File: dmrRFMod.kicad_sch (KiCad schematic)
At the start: 14 parts, among them U2 AX.25 Module (DMR818SU)

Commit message: Added 3D models to all components except DMR module, need to make a 3D model for that one.
Signed-off-by: Logan Tolbert <xem6df@virginia.edu>
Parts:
- R3: footprint R_10OHM:RESC1005X40 -> R_220O:RESC6332X70N
- R4: footprint Resistor_SMD:R_0805_2012Metric -> R_10kO:RESC1005X40N
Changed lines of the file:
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@@
 			)
 		)
-		(property "Footprint" "R_10OHM:RESC1005X40"
+		(property "Footprint" "R_220O:RESC6332X70N"
 			(at 110.236 95.504 90)
 			(effects
@@
 			)
 		)
-		(property "Footprint" "Resistor_SMD:R_0805_2012Metric"
+		(property "Footprint" "R_10kO:RESC1005X40N"
 			(at 129.794 70.866 90)
 			(effects

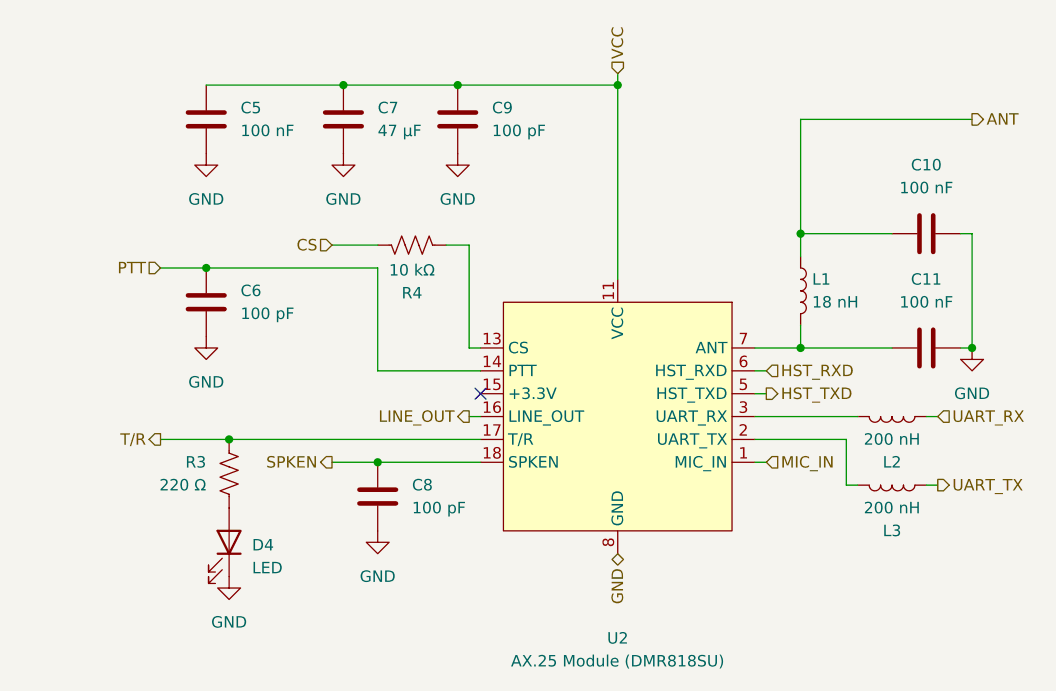
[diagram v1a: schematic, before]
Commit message: removed extraneous connections to the XBee and DMR modules on schematic and PCB.
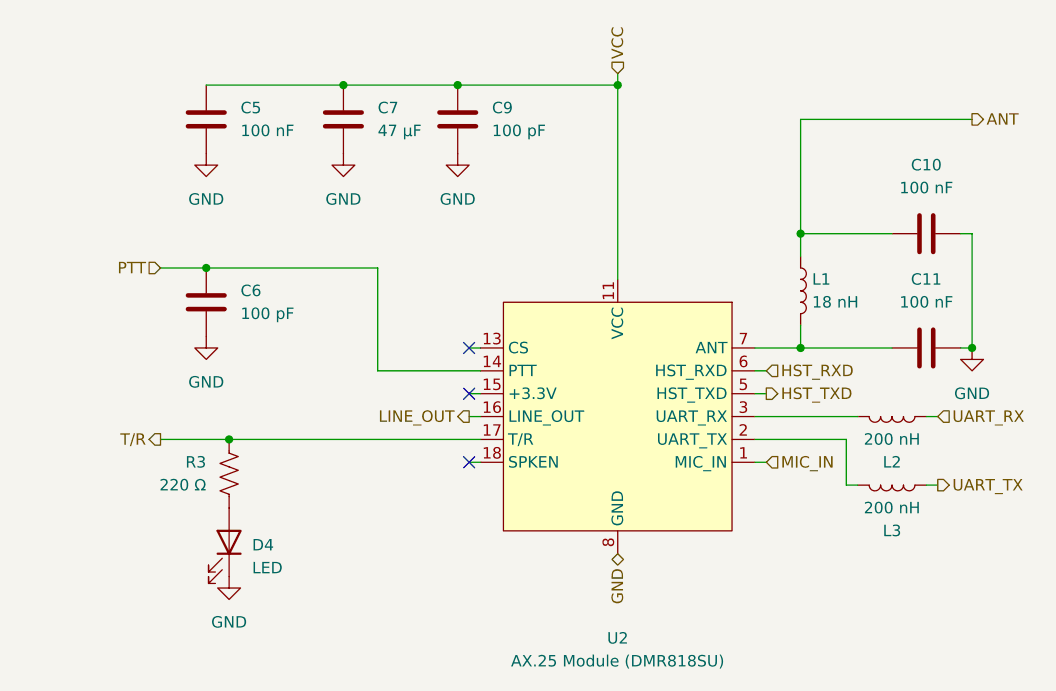
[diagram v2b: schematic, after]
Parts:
- removed C8: 100 pF, C_100pF:CAPC1005X55N, symbol Device:C
- removed R4: 10 kΩ, R_10kO:RESC1005X40N, symbol Device:R_US
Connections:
- net SPKEN: no longer names the net of U2.18 (SPKEN)
- no-connect marks 1 -> 3

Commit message: Added pull-up to CS pin on DMR module.
Signed-off-by: Logan Tolbert <xem6df@virginia.edu>
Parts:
- added R4: 10 kΩ, R_10kO:RESC1005X40N, symbol Device:R_US
- renumbered C11 to C10, C9 to C8, C10 to C9
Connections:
- net VCC: now also R4.1
- net at U2.13 (CS): now also R4.2
- no-connect marks 3 -> 2
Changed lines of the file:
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@@
+	)
+	(junction
+		(at 152.4 67.31)
+		(diameter 0)
+		(color 0 0 0 0)
 	)
 	(junction
@@
 		(at 135.89 86.36)
 	)
-	(no_connect
-		(at 135.89 81.28)
-	)
 	(wire
 		(pts
@@
 	(wire
 		(pts
+			(xy 152.4 67.31) (xy 152.4 73.66)
+		)
+		(stroke
+			(width 0)
+			(type default)
+		)
+	)
+	(wire
+		(pts
 			(xy 101.6 91.44) (xy 109.22 91.44)
 		)
@@
 	(wire
 		(pts
+			(xy 135.89 67.31) (xy 152.4 67.31)
+		)
+		(stroke
+			(width 0)
+			(type default)
+		)
+	)
+	(wire
+		(pts
 			(xy 187.96 96.52) (xy 186.69 96.52)
 		)
@@
 	(wire
 		(pts
+			(xy 135.89 67.31) (xy 135.89 68.58)
+		)
+		(stroke
+			(width 0)
+			(type default)
+		)
+	)
+	(wire
+		(pts
 			(xy 191.77 68.58) (xy 190.5 68.58)
 		)
@@
 	(wire
 		(pts
+			(xy 135.89 76.2) (xy 135.89 81.28)
+		)
+		(stroke
+			(width 0)
+			(type default)
+		)
+	)
+	(wire
+		(pts
 			(xy 121.92 52.07) (xy 134.62 52.07)
 		)
@@
 	(wire
 		(pts
-			(xy 152.4 52.07) (xy 152.4 73.66)
+			(xy 152.4 52.07) (xy 152.4 67.31)
 		)
 		(stroke
@@
 		(dnp no)
 		(fields_autoplaced yes)
-		(property "Reference" "#PWR027"
+		(property "Reference" "#PWR026"
 			(at 191.77 87.63 0)
 			(effects
@@
 			(project ""
 				(path "/b0bd204d-ca77-4624-acd2-31813bf00a6c/981163d3-3d7a-4bc9-948c-2bbe4a7c373b"
-					(reference "#PWR027")
+					(reference "#PWR026")
 					(unit 1)
 				)
@@
 		(dnp no)
 		(fields_autoplaced yes)
-		(property "Reference" "C11"
+		(property "Reference" "C10"
 			(at 186.69 73.66 90)
 			(effects
@@
 			(project ""
 				(path "/b0bd204d-ca77-4624-acd2-31813bf00a6c/981163d3-3d7a-4bc9-948c-2bbe4a7c373b"
-					(reference "C11")
+					(reference "C10")
 					(unit 1)
 				)
@@
 		(dnp no)
 		(fields_autoplaced yes)
-		(property "Reference" "C10"
+		(property "Reference" "C9"
 			(at 186.69 60.96 90)
 			(effects
@@
 			(project ""
 				(path "/b0bd204d-ca77-4624-acd2-31813bf00a6c/981163d3-3d7a-4bc9-948c-2bbe4a7c373b"
-					(reference "C10")
+					(reference "C9")
+					(unit 1)
+				)
+			)
+		)
+	)
+	(symbol
+		(lib_id "Device:R_US")
+		(at 135.89 72.39 0)
+		(unit 1)
+		(exclude_from_sim no)
+		(in_bom yes)
+		(on_board yes)
+		(dnp no)
+		(fields_autoplaced yes)
+		(property "Reference" "R4"
+			(at 138.43 71.1199 0)
+			(effects
+				(font
+					(size 1.27 1.27)
+				)
+				(justify left)
+			)
+		)
+		(property "Value" "10 kΩ"
+			(at 138.43 73.6599 0)
+			(effects
+				(font
+					(size 1.27 1.27)
+				)
+				(justify left)
+			)
+		)
+		(property "Footprint" "R_10kO:RESC1005X40N"
+			(at 136.906 72.644 90)
+			(effects
+				(font
+					(size 1.27 1.27)
+				)
+				(hide yes)
+			)
+		)
+		(property "Datasheet" "~"
+			(at 135.89 72.39 0)
+			(effects
+				(font
+					(size 1.27 1.27)
+				)
+				(hide yes)
+			)
+		)
+		(property "Description" "Resistor, US symbol"
+			(at 135.89 72.39 0)
+			(effects
+				(font
+					(size 1.27 1.27)
+				)
+				(hide yes)
+			)
+		)
+		(pin "2"
+		)
+		(pin "1"
+		)
+		(instances
+			(project ""
+				(path "/b0bd204d-ca77-4624-acd2-31813bf00a6c/981163d3-3d7a-4bc9-948c-2bbe4a7c373b"
+					(reference "R4")
 					(unit 1)
 				)
@@
 		(dnp no)
 		(fields_autoplaced yes)
-		(property "Reference" "#PWR026"
+		(property "Reference" "#PWR025"
 			(at 134.62 66.04 0)
 			(effects
@@
 			(project "COMM"
 				(path "/b0bd204d-ca77-4624-acd2-31813bf00a6c/981163d3-3d7a-4bc9-948c-2bbe4a7c373b"
-					(reference "#PWR026")
+					(reference "#PWR025")
 					(unit 1)
 				)
@@
 		(dnp no)
 		(fields_autoplaced yes)
-		(property "Reference" "C9"
+		(property "Reference" "C8"
 			(at 138.43 54.6099 0)
 			(effects
@@
 			(project ""
 				(path "/b0bd204d-ca77-4624-acd2-31813bf00a6c/981163d3-3d7a-4bc9-948c-2bbe4a7c373b"
-					(reference "C9")
+					(reference "C8")
 					(unit 1)
 				)

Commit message: Addressed most comments from McPherson, modified schematic.
Signed-off-by: Logan Tolbert <xem6df@virginia.edu>
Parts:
- removed L2, L3: 200 nH, CLT32_R20_200nH:IND_CLT32-R20, symbol Device:L
- removed R4: 10 kΩ, R_10kO:RESC1005X40N, symbol Device:R_US
- D4: value LED -> BLU_TR_DMR
- R4: renamed from R3; value 220 Ω -> 80 Ω
- U2: value AX.25 Module (DMR818SU) -> DMR Module (DMR818S-5W)
- renumbered C9 to C10, C10 to C11, C5 to C6, C6 to C7, C7 to C8, C8 to C9
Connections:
- net UART_RX: now also U2.3 (UART_RX)
- net UART_TX: now also U2.2 (UART_TX)
- net +3.3V: now reaches U2.13 (CS)
- net HST_RXD: no longer names the net of U2.6 (HST_RXD)
- net HST_TXD: no longer names the net of U2.5 (HST_TXD)
- no-connect marks 2 -> 4
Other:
- moved on the sheet: C10, C11, C6, C7, C8, C9, D4, L1, R4

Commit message: Finalized board design, updated DMR module to DMR818S-5W exact dimensions, rerouted PCB according to McPherson's comments. Added TLV61047 5V to 8V booster module.
Signed-off-by: Logan Tolbert <xem6df@virginia.edu>
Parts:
- U2: footprint DMR818S:DMR818SU -> DMR818S:DMR818S-5W
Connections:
- net GND: now also U2.21 (GND)
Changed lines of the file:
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@@
 			)
 		)
-		(property "Footprint" "DMR818S:DMR818SU"
+		(property "Footprint" "DMR818S:DMR818S-5W"
 			(at 165.1 77.47 0)
 			(effects
@@
 		(pin "14"
 		)
+		(pin "21"
+		)
 		(instances

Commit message: Removed extranous capacitors and resistors off of DMR module. Final Board Design, check one more time before ordering parts.
Signed-off-by: Logan Tolbert <xem6df@virginia.edu>
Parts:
- removed C10, C11: 100 nF, C_100nF:CAPC1608X90, symbol Device:C
- removed C7: 100 pF, C_100pF:CAPC1005X55N, symbol Device:C
- removed L1: 18 nH, LQG15HS18NJ02D_18nH:INDC1005X55N, symbol Device:L
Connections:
- net ANT: now also U2.7 (ANT)

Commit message: Final COMM board design as of Feb 12 2026, ready to order.
Signed-off-by: Logan Tolbert <xem6df@virginia.edu>
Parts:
- D4: value BLU_TR_DMR -> YLW_TR_DMR
- R4: value 80 Ω -> 140 Ω; footprint R_220O:RESC6332X70N -> R_140O:RESC3216X70N
- renumbered C8 to C7, C9 to C8
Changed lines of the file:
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@@
 			)
 		)
-		(property "Value" "80 Ω"
+		(property "Value" "140 Ω"
 			(at 118.11 97.7899 0)
 			(effects
@@
 			)
 		)
-		(property "Footprint" "R_220O:RESC6332X70N"
+		(property "Footprint" "R_140O:RESC3216X70N"
 			(at 121.666 96.774 90)
 			(effects
@@
 		(dnp no)
 		(fields_autoplaced yes)
-		(property "Reference" "C8"
+		(property "Reference" "C7"
 			(at 107.95 58.4199 0)
 			(effects
@@
 			(project ""
 				(path "/b0bd204d-ca77-4624-acd2-31813bf00a6c/981163d3-3d7a-4bc9-948c-2bbe4a7c373b"
-					(reference "C8")
+					(reference "C7")
 					(unit 1)
 				)
@@
 		(dnp no)
 		(fields_autoplaced yes)
-		(property "Reference" "#PWR028"
+		(property "Reference" "#PWR027"
 			(at 116.84 69.85 0)
 			(effects
@@
 			(project "COMM"
 				(path "/b0bd204d-ca77-4624-acd2-31813bf00a6c/981163d3-3d7a-4bc9-948c-2bbe4a7c373b"
-					(reference "#PWR028")
+					(reference "#PWR027")
 					(unit 1)
 				)
@@
 		(dnp no)
 		(fields_autoplaced yes)
-		(property "Reference" "#PWR030"
+		(property "Reference" "#PWR029"
 			(at 135.89 83.82 0)
 			(effects
@@
 			(project ""
 				(path "/b0bd204d-ca77-4624-acd2-31813bf00a6c/981163d3-3d7a-4bc9-948c-2bbe4a7c373b"
-					(reference "#PWR030")
+					(reference "#PWR029")
 					(unit 1)
 				)
@@
 		(dnp no)
 		(fields_autoplaced yes)
-		(property "Reference" "#PWR027"
+		(property "Reference" "#PWR026"
 			(at 104.14 69.85 0)
 			(effects
@@
 			(project "COMM"
 				(path "/b0bd204d-ca77-4624-acd2-31813bf00a6c/981163d3-3d7a-4bc9-948c-2bbe4a7c373b"
-					(reference "#PWR027")
+					(reference "#PWR026")
 					(unit 1)
 				)
@@
 			)
 		)
-		(property "Value" "BLU_TR_DMR"
+		(property "Value" "YLW_TR_DMR"
 			(at 123.19 106.9974 90)
 			(effects
@@
 		(dnp no)
 		(fields_autoplaced yes)
-		(property "Reference" "#PWR029"
+		(property "Reference" "#PWR028"
 			(at 120.65 114.3 0)
 			(effects
@@
 			(project ""
 				(path "/b0bd204d-ca77-4624-acd2-31813bf00a6c/981163d3-3d7a-4bc9-948c-2bbe4a7c373b"
-					(reference "#PWR029")
+					(reference "#PWR028")
 					(unit 1)
 				)
@@
 		(dnp no)
 		(fields_autoplaced yes)
-		(property "Reference" "C9"
+		(property "Reference" "C8"
 			(at 120.65 58.4199 0)
 			(effects
@@
 			(project ""
 				(path "/b0bd204d-ca77-4624-acd2-31813bf00a6c/981163d3-3d7a-4bc9-948c-2bbe4a7c373b"
-					(reference "C9")
-					(unit 1)
-				)
+					(reference "C8")
+					(unit 1)
+				)

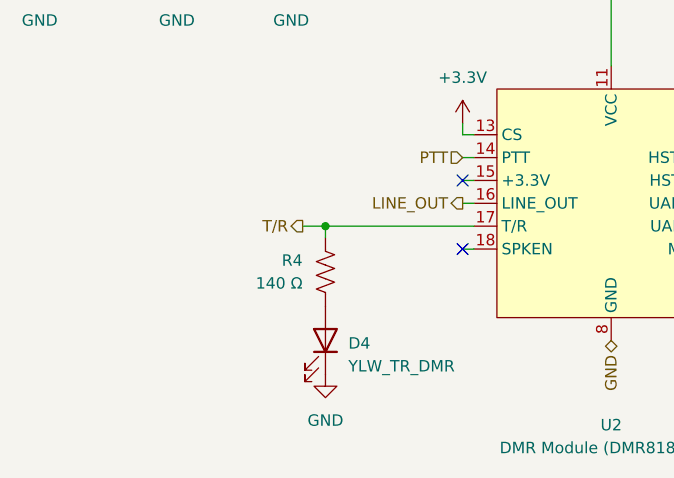
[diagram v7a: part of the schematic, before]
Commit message: Updated LEDs and associated resistors on board. COMM board is ready to be reordered.
Signed-off-by: Logan Tolbert <xem6df@virginia.edu>
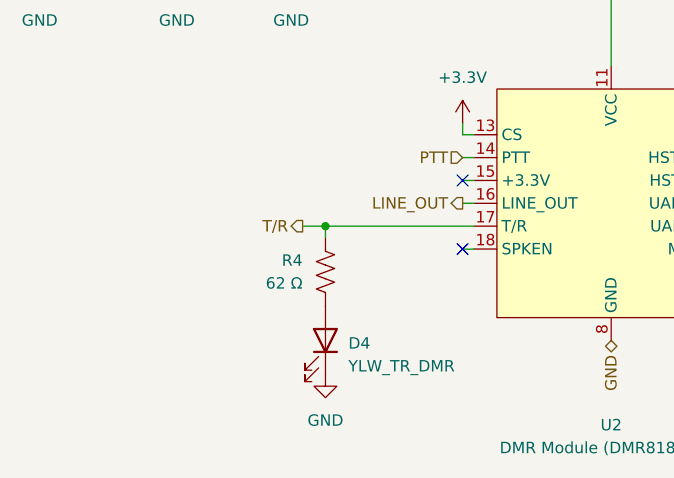
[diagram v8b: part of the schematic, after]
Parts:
- D4: footprint LED_THT:LED_D3.0mm -> LED_THT:LED_D5.0mm
- R4: value 140 Ω -> 62 Ω; footprint R_140O:RESC3216X70N -> Resistor_SMD:R_0603_1608Metric
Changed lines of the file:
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@@
 			)
 		)
-		(property "Value" "140 Ω"
+		(property "Value" "62 Ω"
 			(at 118.11 97.7899 0)
 			(effects
@@
 			)
 		)
-		(property "Footprint" "R_140O:RESC3216X70N"
+		(property "Footprint" "Resistor_SMD:R_0603_1608Metric"
 			(at 121.666 96.774 90)
 			(effects
@@
 			)
 		)
-		(property "Footprint" "LED_THT:LED_D3.0mm"
+		(property "Footprint" "LED_THT:LED_D5.0mm"
 			(at 120.65 104.14 0)
 			(effects
